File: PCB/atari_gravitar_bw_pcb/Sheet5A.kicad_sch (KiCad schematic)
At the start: 124 parts, among them Q2 2N6044, Q3 2N6044, Q4 2N6044

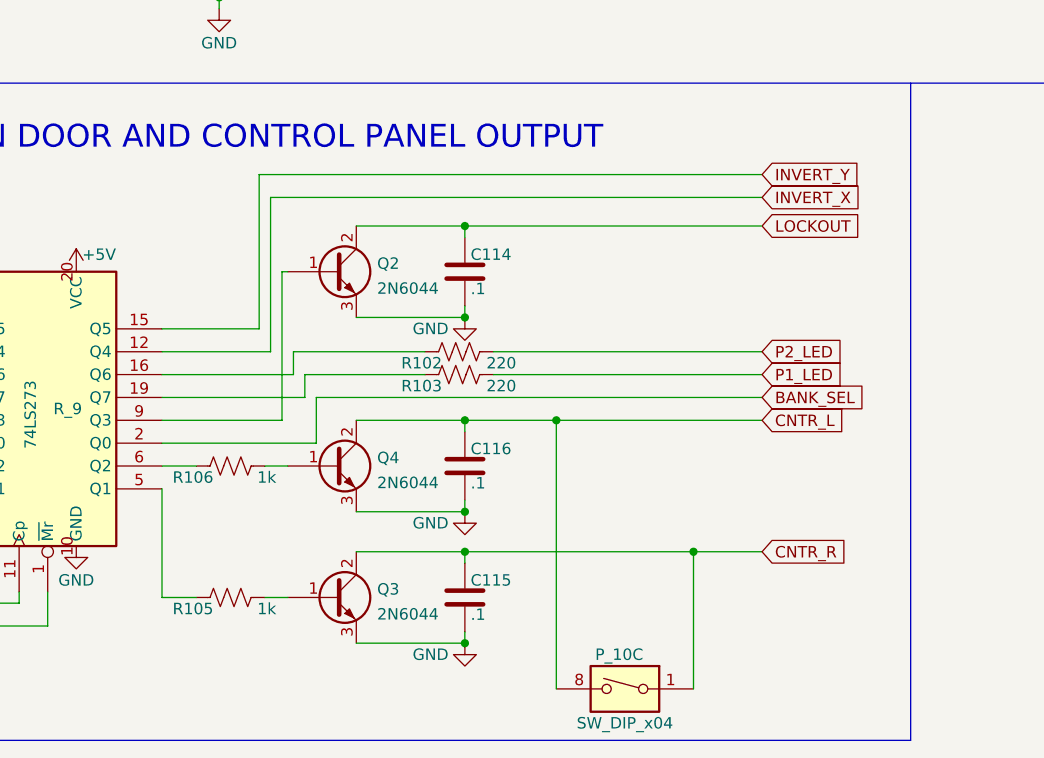
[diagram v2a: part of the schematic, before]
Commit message: Finished sheet 5B
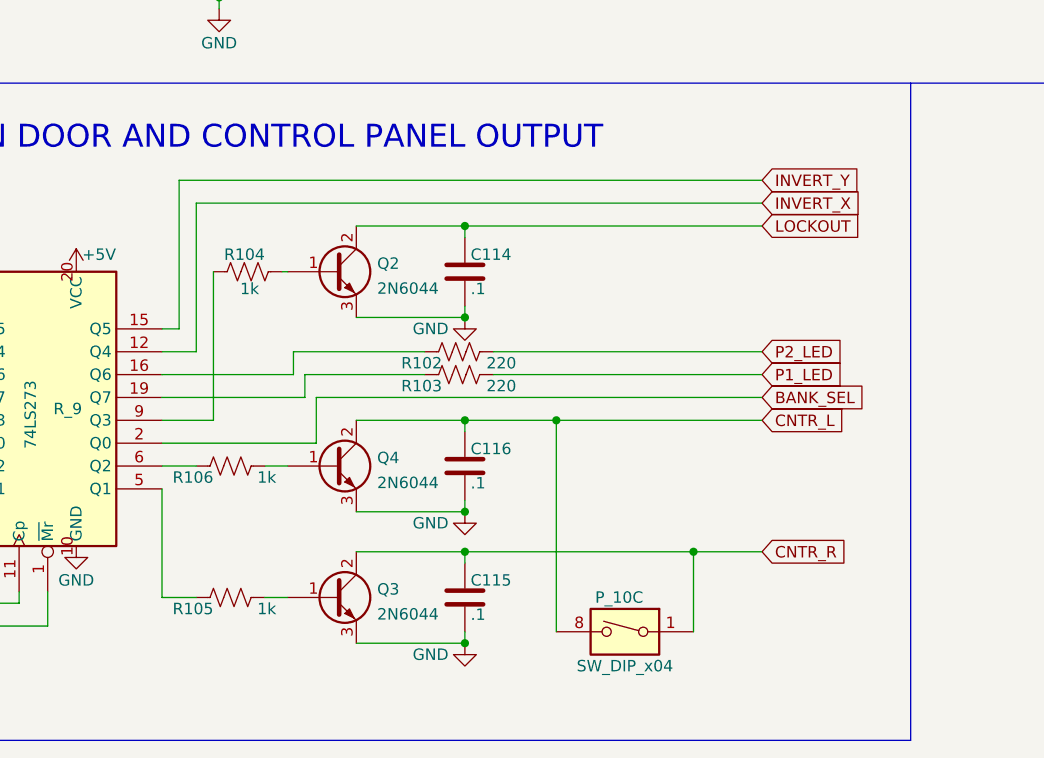
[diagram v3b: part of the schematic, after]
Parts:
- added R104: 1k, symbol Device:R_US
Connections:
- net at R_9.9 (Q3): now also R104.1; no longer Q2.1 (B)
- new net: Q2.1 (B), R104.2
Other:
- moved on the sheet: P_10C
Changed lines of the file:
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@@
     (stroke (width 0) (type default) (color 0 0 0 0))
   )
-  (wire (pts (xy 256.54 245.745) (xy 256.54 275.59))
+  (wire (pts (xy 256.54 245.745) (xy 256.54 269.24))
     (stroke (width 0) (type default) (color 0 0 0 0))
   )
@@
     (stroke (width 0) (type default) (color 0 0 0 0))
   )
-  (wire (pts (xy 212.725 238.125) (xy 224.79 238.125))
-    (stroke (width 0) (type default) (color 0 0 0 0))
-  )
   (wire (pts (xy 51.435 208.28) (xy 51.435 211.455))
     (stroke (width 0) (type default) (color 0 0 0 0))
@@
     (stroke (width 0) (type default) (color 0 0 0 0))
   )
+  (wire (pts (xy 218.44 245.745) (xy 212.725 245.745))
+    (stroke (width 0) (type default) (color 0 0 0 0))
+  )
   (wire (pts (xy 59.055 140.335) (xy 59.055 151.13))
     (stroke (width 0) (type default) (color 0 0 0 0))
@@
     (stroke (width 0) (type default) (color 0 0 0 0))
   )
-  (wire (pts (xy 212.725 235.585) (xy 223.52 235.585))
-    (stroke (width 0) (type default) (color 0 0 0 0))
-  )
   (wire (pts (xy 60.325 94.615) (xy 57.785 94.615))
     (stroke (width 0) (type default) (color 0 0 0 0))
@@
     (stroke (width 0) (type default) (color 0 0 0 0))
   )
+  (wire (pts (xy 216.535 221.615) (xy 216.535 238.125))
+    (stroke (width 0) (type default) (color 0 0 0 0))
+  )
   (wire (pts (xy 57.785 78.74) (xy 66.04 78.74))
     (stroke (width 0) (type default) (color 0 0 0 0))
@@
     (stroke (width 0) (type default) (color 0 0 0 0))
   )
+  (wire (pts (xy 212.725 235.585) (xy 214.63 235.585))
+    (stroke (width 0) (type default) (color 0 0 0 0))
+  )
   (wire (pts (xy 94.615 195.58) (xy 94.615 205.74))
     (stroke (width 0) (type default) (color 0 0 0 0))
@@
     (stroke (width 0) (type default) (color 0 0 0 0))
   )
-  (wire (pts (xy 224.79 220.98) (xy 279.4 220.98))
+  (wire (pts (xy 216.535 221.615) (xy 279.4 221.615))
     (stroke (width 0) (type default) (color 0 0 0 0))
   )
@@
     (stroke (width 0) (type default) (color 0 0 0 0))
   )
+  (wire (pts (xy 216.535 238.125) (xy 212.725 238.125))
+    (stroke (width 0) (type default) (color 0 0 0 0))
+  )
   (wire (pts (xy 217.805 115.57) (xy 217.805 127.635))
     (stroke (width 0) (type default) (color 0 0 0 0))
@@
     (stroke (width 0) (type default) (color 0 0 0 0))
   )
-  (wire (pts (xy 223.52 218.44) (xy 279.4 218.44))
+  (wire (pts (xy 214.63 219.075) (xy 279.4 219.075))
     (stroke (width 0) (type default) (color 0 0 0 0))
   )
@@
     (stroke (width 0) (type default) (color 0 0 0 0))
   )
-  (wire (pts (xy 224.79 238.125) (xy 224.79 220.98))
-    (stroke (width 0) (type default) (color 0 0 0 0))
-  )
   (wire (pts (xy 266.065 172.72) (xy 266.065 187.325))
     (stroke (width 0) (type default) (color 0 0 0 0))
@@
     (stroke (width 0) (type default) (color 0 0 0 0))
   )
-  (wire (pts (xy 271.78 260.35) (xy 271.78 275.59))
+  (wire (pts (xy 271.78 260.35) (xy 271.78 269.24))
     (stroke (width 0) (type default) (color 0 0 0 0))
   )
@@
     (stroke (width 0) (type default) (color 0 0 0 0))
   )
-  (wire (pts (xy 226.06 245.745) (xy 212.725 245.745))
-    (stroke (width 0) (type default) (color 0 0 0 0))
-  )
   (wire (pts (xy 144.145 193.04) (xy 152.4 193.04))
     (stroke (width 0) (type default) (color 0 0 0 0))
@@
     (stroke (width 0) (type default) (color 0 0 0 0))
   )
-  (wire (pts (xy 223.52 235.585) (xy 223.52 218.44))
+  (wire (pts (xy 214.63 235.585) (xy 214.63 219.075))
     (stroke (width 0) (type default) (color 0 0 0 0))
   )
@@
     (stroke (width 0) (type default) (color 0 0 0 0))
   )
-  (wire (pts (xy 226.06 229.235) (xy 226.06 245.745))
-    (stroke (width 0) (type default) (color 0 0 0 0))
-  )
   (wire (pts (xy 225.425 105.41) (xy 222.885 105.41))
     (stroke (width 0) (type default) (color 0 0 0 0))
@@
   )
   (wire (pts (xy 41.91 81.28) (xy 60.325 81.28))
+    (stroke (width 0) (type default) (color 0 0 0 0))
+  )
+  (wire (pts (xy 218.44 229.235) (xy 218.44 245.745))
     (stroke (width 0) (type default) (color 0 0 0 0))
   )
@@
     )
   )
-  (global_label "INVERT_Y" (shape input) (at 279.4 218.44 0) (fields_autoplaced)
-    (effects (font (size 1.27 1.27)) (justify left))
-    (property "Intersheet References" "${INTERSHEET_REFS}" (id 0) (at 290.2798 218.3606 0)
+  (global_label "INVERT_Y" (shape input) (at 279.4 219.075 0) (fields_autoplaced)
+    (effects (font (size 1.27 1.27)) (justify left))
+    (property "Intersheet References" "${INTERSHEET_REFS}" (id 0) (at 290.2798 218.9956 0)
       (effects (font (size 1.27 1.27)) (justify left) hide)
     )
@@
     )
   )
-  (global_label "INVERT_X" (shape input) (at 279.4 220.98 0) (fields_autoplaced)
-    (effects (font (size 1.27 1.27)) (justify left))
-    (property "Intersheet References" "${INTERSHEET_REFS}" (id 0) (at 290.4007 220.9006 0)
+  (global_label "INVERT_X" (shape input) (at 279.4 221.615 0) (fields_autoplaced)
+    (effects (font (size 1.27 1.27)) (justify left))
+    (property "Intersheet References" "${INTERSHEET_REFS}" (id 0) (at 290.4007 221.5356 0)
       (effects (font (size 1.27 1.27)) (justify left) hide)
     )
@@
       (effects (font (size 1.27 1.27)) (justify right) hide)
     )
+  )
+  (symbol (lib_id "Device:R_US") (at 222.25 229.235 90) (unit 1)
+    (in_bom yes) (on_board yes)
+    (property "Reference" "R104" (id 0) (at 224.155 227.33 90)
+      (effects (font (size 1.27 1.27)) (justify left))
+    )
+    (property "Value" "1k" (id 1) (at 223.52 231.14 90)
+      (effects (font (size 1.27 1.27)) (justify left))
+    )
+    (property "Footprint" "" (id 2) (at 222.504 228.219 90)
+      (effects (font (size 1.27 1.27)) hide)
+    )
+    (property "Datasheet" "~" (id 3) (at 222.25 229.235 0)
+      (effects (font (size 1.27 1.27)) hide)
+    )
+    (pin "1")
+    (pin "2")
   )
   (symbol (lib_id "Device:R_US") (at 324.485 107.95 90) (unit 1)
@@
     (pin "2")
   )
-  (symbol (lib_id "atari:SW_DIP_x04") (at 264.16 275.59 0) (mirror y) (unit 3)
-    (in_bom yes) (on_board yes)
-    (property "Reference" "P_10" (id 0) (at 263.525 271.78 0))
-    (property "Value" "SW_DIP_x04" (id 1) (at 264.16 279.4 0))
-    (property "Footprint" "" (id 2) (at 264.16 275.59 0)
-      (effects (font (size 1.27 1.27)) hide)
-    )
-    (property "Datasheet" "" (id 3) (at 264.16 275.59 0)
-      (effects (font (size 1.27 1.27)) hide)
-    )
+  (symbol (lib_id "atari:SW_DIP_x04") (at 264.16 269.24 0) (mirror y) (unit 3)
+    (in_bom yes) (on_board yes)
+    (property "Reference" "P_10" (id 0) (at 263.525 265.43 0))
+    (property "Value" "SW_DIP_x04" (id 1) (at 264.16 273.05 0))
+    (property "Footprint" "" (id 2) (at 264.16 269.24 0)
+      (effects (font (size 1.27 1.27)) hide)
+    )
+    (property "Datasheet" "" (id 3) (at 264.16 269.24 0)
+      (effects (font (size 1.27 1.27)) hide)
+    )
